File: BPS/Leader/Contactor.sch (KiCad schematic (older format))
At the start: 20 parts, among them J8 ContactorConn, Q1 NTR4003NT1G, Q2 VND5N07-E, U8 SI8261ABC-IS, U9 BAS70-04

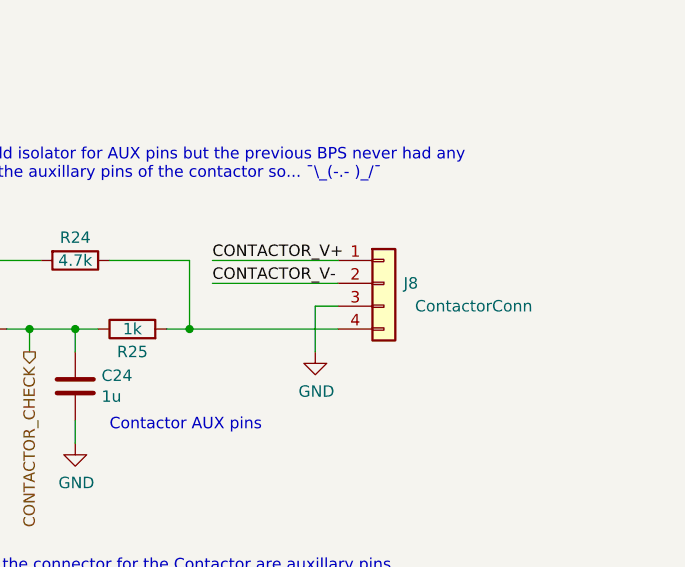
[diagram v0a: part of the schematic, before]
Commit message: Places most components of leader board in their respective locations with nothing traced
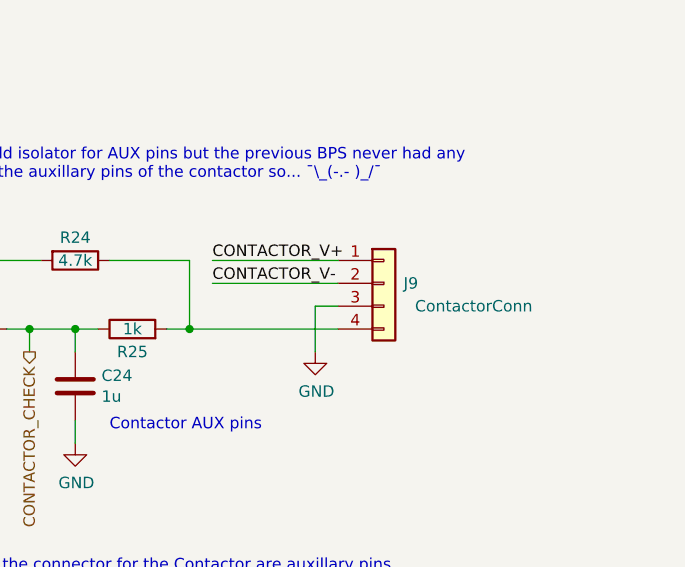
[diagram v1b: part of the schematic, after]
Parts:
- renumbered J8 to J9
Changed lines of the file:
@@
 $EndDescr
 $Comp
-L Connector_Generic:Conn_01x04 J8
+L Connector_Generic:Conn_01x04 J9
 U 1 1 5C2DA595
 P 10050 3500
-F 0 "J8" H 10200 3500 50  0000 R CNN
+F 0 "J9" H 10200 3500 50  0000 R CNN
 F 1 "ContactorConn" H 10700 3400 50  0000 R CNN
 F 2 "UTSVT_Connectors:Molex_MicroFit3.0_1x4xP3.00mm_PolarizingPeg_Vertical" H 10050 3500 50  0001 C CNN

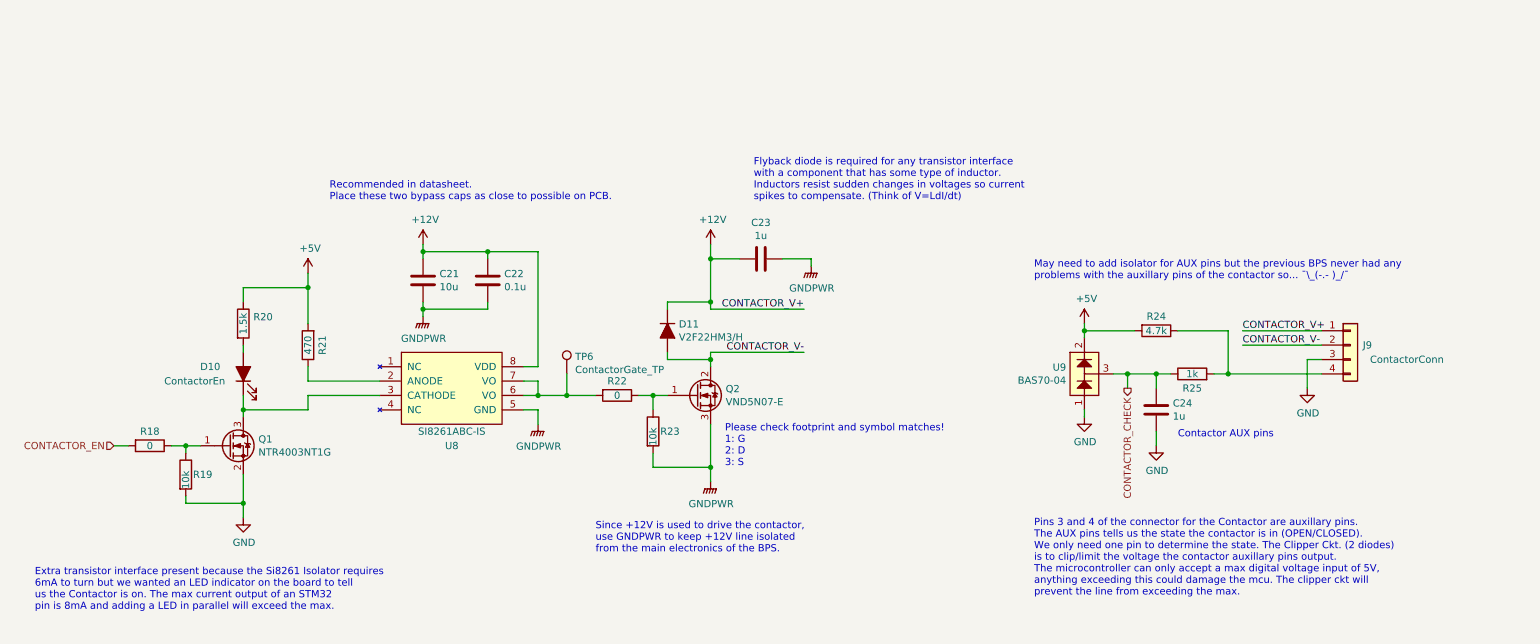
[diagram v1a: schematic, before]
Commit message: Adds power planes
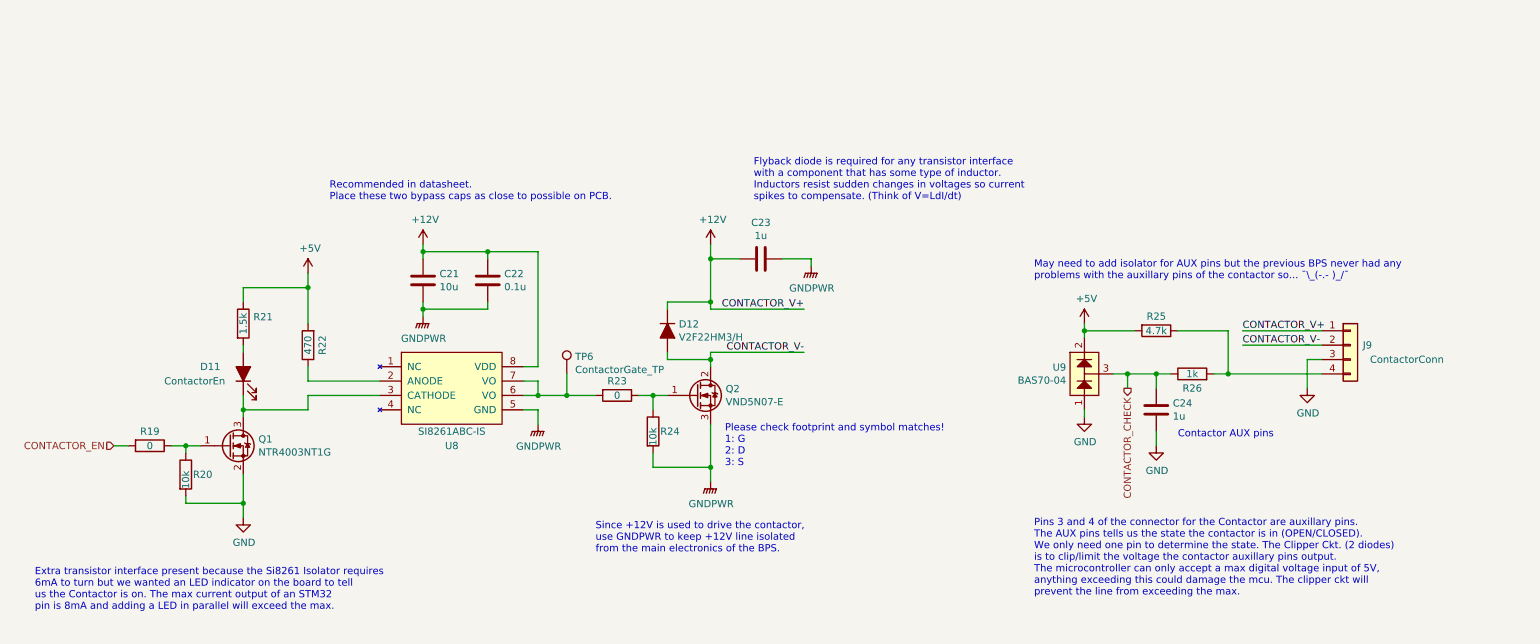
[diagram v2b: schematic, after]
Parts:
- renumbered D10 to D11, D11 to D12, R18 to R19, R19 to R20, R20 to R21, R21 to R22, R22 to R23, R23 to R24, R24 to R25, R25 to R26
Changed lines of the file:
@@
 $EndComp
 $Comp
-L Device:R R25
+L Device:R R26
 U 1 1 5C302C24
 P 8950 3700
-F 0 "R25" V 8850 3700 50  0000 C CNN
+F 0 "R26" V 8850 3700 50  0000 C CNN
 F 1 "1k" V 8950 3700 50  0000 C CNN
 F 2 "Resistor_SMD:R_0805_2012Metric" V 8880 3700 50  0001 C CNN
@@
 CONTACTOR_V-
 $Comp
-L Device:R R23
+L Device:R R24
 U 1 1 5C30E2C4
 P 5200 4100
-F 0 "R23" H 5250 4100 50  0000 L CNN
+F 0 "R24" H 5250 4100 50  0000 L CNN
 F 1 "10k" V 5200 4000 50  0000 L CNN
 F 2 "Resistor_SMD:R_0805_2012Metric" V 5130 4100 50  0001 C CNN
@@
 Connection ~ 5600 4350
 $Comp
-L Device:R R22
+L Device:R R23
 U 1 1 5C30EC57
 P 4950 3850
-F 0 "R22" V 4850 3850 50  0000 C CNN
+F 0 "R23" V 4850 3850 50  0000 C CNN
 F 1 "0" V 4950 3850 50  0000 C CNN
 F 2 "Resistor_SMD:R_0805_2012Metric" V 4880 3850 50  0001 C CNN
@@
 	4400 3950 4300 3950
 $Comp
-L Device:R R21
+L Device:R R22
 U 1 1 5C3152A3
 P 2800 3500
-F 0 "R21" V 2700 3500 50  0000 C CNN
+F 0 "R22" V 2700 3500 50  0000 C CNN
 F 1 "470" V 2800 3500 50  0000 C CNN
 F 2 "Resistor_SMD:R_0805_2012Metric" V 2730 3500 50  0001 C CNN
@@
 Please check footprint and symbol matches!\n1: G\n2: D\n3: S
 $Comp
-L Device:D_ALT D11
+L Device:D_ALT D12
 U 1 1 5C31D45E
 P 5300 3400
-F 0 "D11" V 5254 3479 50  0000 L CNN
+F 0 "D12" V 5254 3479 50  0000 L CNN
 F 1 "V2F22HM3/H" V 5345 3479 50  0000 L CNN
 F 2 "UTSVT_Passive:V2F22HM" H 5300 3400 50  0001 C CNN
@@
 Connection ~ 4600 3850
 $Comp
-L Device:R R20
+L Device:R R21
 U 1 1 5C381FF3
 P 2350 3350
-F 0 "R20" H 2420 3396 50  0000 L CNN
+F 0 "R21" H 2420 3396 50  0000 L CNN
 F 1 "1.5k" V 2350 3350 50  0000 C CNN
 F 2 "Resistor_SMD:R_0805_2012Metric" V 2280 3350 50  0001 C CNN
@@
 	2350 3200 2350 3100
 $Comp
-L Device:LED_ALT D10
+L Device:LED_ALT D11
 U 1 1 5C382DF7
 P 2350 3700
-F 0 "D10" V 2400 4000 50  0000 R CNN
+F 0 "D11" V 2400 4000 50  0000 R CNN
 F 1 "ContactorEn" V 2300 4250 50  0000 R CNN
 F 2 "LED_SMD:LED_0805_2012Metric" H 2350 3700 50  0001 C CNN
@@
 	2350 3550 2350 3500
 $Comp
-L Device:R R24
+L Device:R R25
 U 1 1 5C3945DD
 P 8700 3400
-F 0 "R24" V 8600 3400 50  0000 C CNN
+F 0 "R25" V 8600 3400 50  0000 C CNN
 F 1 "4.7k" V 8700 3400 50  0000 C CNN
 F 2 "Resistor_SMD:R_0805_2012Metric" V 8630 3400 50  0001 C CNN
@@
 Connection ~ 2800 3100
 $Comp
-L Device:R R18
+L Device:R R19
 U 1 1 5C3FA547
 P 1700 4200
-F 0 "R18" V 1600 4200 50  0000 C CNN
+F 0 "R19" V 1600 4200 50  0000 C CNN
 F 1 "0" V 1700 4200 50  0000 C CNN
 F 2 "Resistor_SMD:R_0805_2012Metric" V 1630 4200 50  0001 C CNN
@@
 $EndComp
 $Comp
-L Device:R R19
+L Device:R R20
 U 1 1 5C400FAD
 P 1950 4400
-F 0 "R19" H 2000 4400 50  0000 L CNN
+F 0 "R20" H 2000 4400 50  0000 L CNN
 F 1 "10k" V 1950 4300 50  0000 L CNN
 F 2 "Resistor_SMD:R_0805_2012Metric" V 1880 4400 50  0001 C CNN

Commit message: Finished leader board
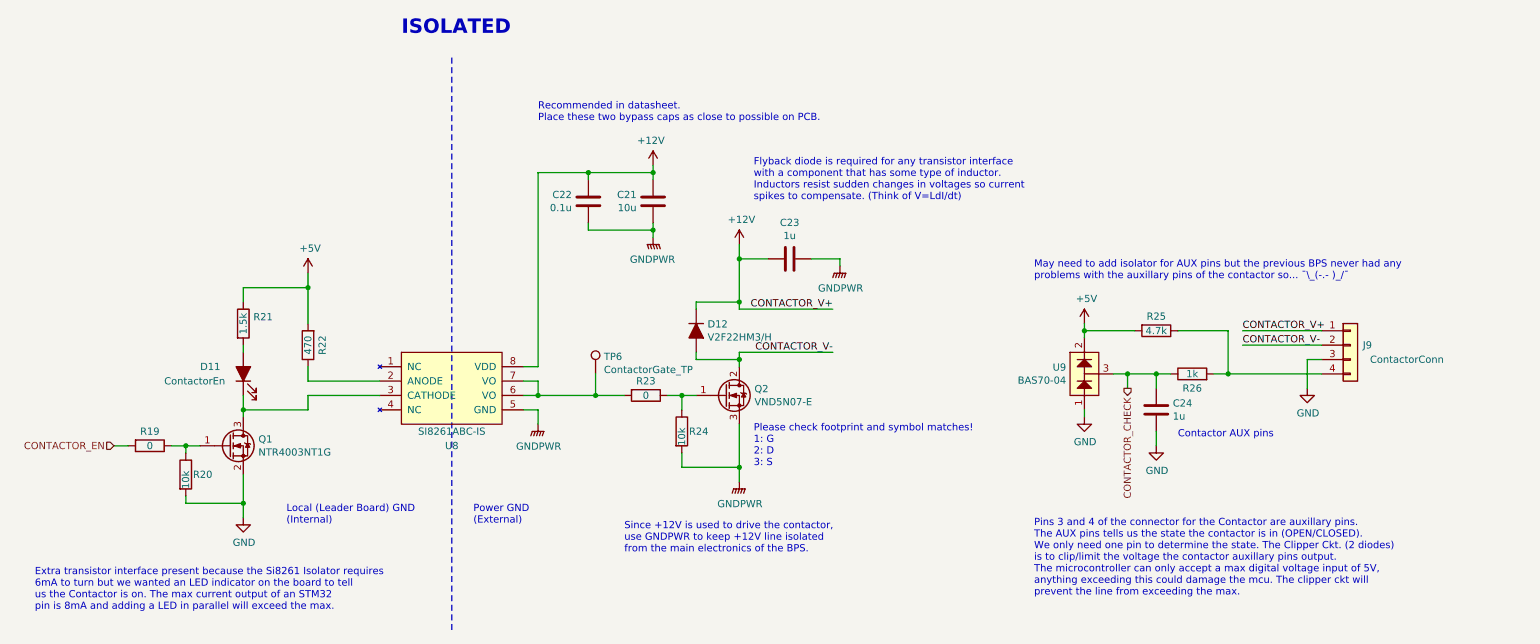
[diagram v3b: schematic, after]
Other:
- note added: "ISOLATED"
- note added: "Local (Leader Board) GND\n(Internal)"
- note added: "Power GND\n(External)"
- moved on the sheet: C21, C22, C23, D12, Q2, R23, R24, TP6

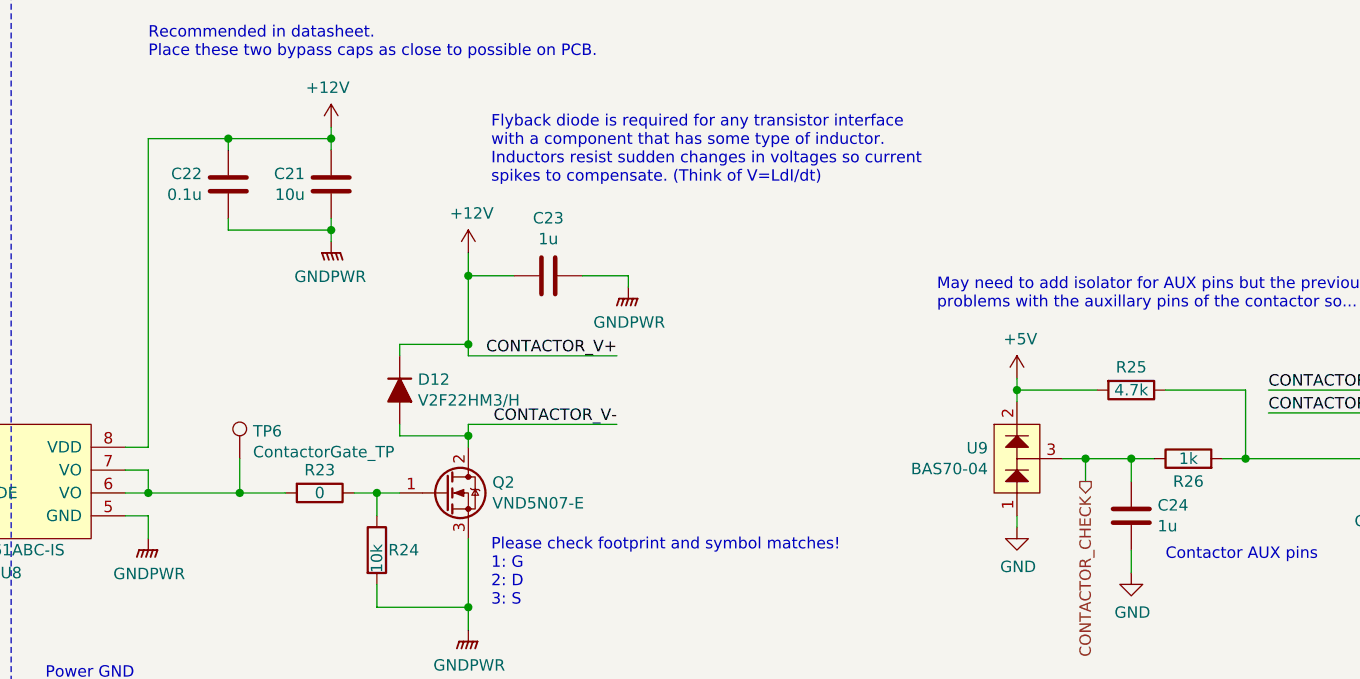
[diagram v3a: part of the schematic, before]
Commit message: Simplifies dc-dc converter schematics
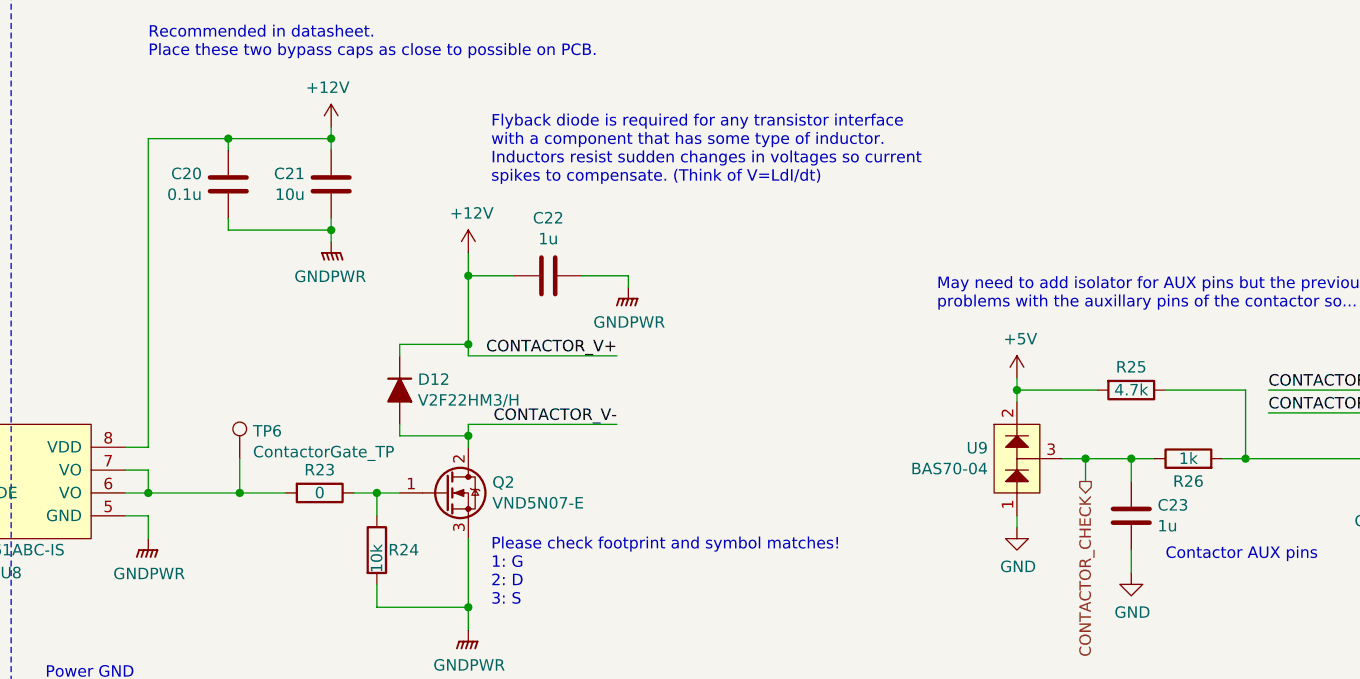
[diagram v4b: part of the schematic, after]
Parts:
- renumbered C22 to C20, C23 to C22, C24 to C23
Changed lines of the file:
@@
 $EndComp
 $Comp
-L power:GND #PWR062
+L power:GND #PWR061
 U 1 1 5C30292A
 P 9750 3800
-F 0 "#PWR062" H 9750 3550 50  0001 C CNN
+F 0 "#PWR061" H 9750 3550 50  0001 C CNN
 F 1 "GND" H 9755 3627 50  0000 C CNN
 F 2 "" H 9750 3800 50  0001 C CNN
@@
 	9850 3700 9200 3700
 $Comp
-L Device:C C24
+L Device:C C23
 U 1 1 5C3030F2
 P 8700 3950
-F 0 "C24" H 8815 3996 50  0000 L CNN
+F 0 "C23" H 8815 3996 50  0000 L CNN
 F 1 "1u" H 8815 3905 50  0000 L CNN
 F 2 "Capacitor_SMD:C_0805_2012Metric" H 8738 3800 50  0001 C CNN
@@
 	8700 4200 8700 4100
 $Comp
-L power:GND #PWR061
+L power:GND #PWR060
 U 1 1 5C304D16
 P 8700 4200
-F 0 "#PWR061" H 8700 3950 50  0001 C CNN
+F 0 "#PWR060" H 8700 3950 50  0001 C CNN
 F 1 "GND" H 8705 4027 50  0000 C CNN
 F 2 "" H 8700 4200 50  0001 C CNN
@@
 Connection ~ 8700 3700
 $Comp
-L power:GND #PWR060
+L power:GND #PWR059
 U 1 1 5C305432
 P 8200 4000
-F 0 "#PWR060" H 8200 3750 50  0001 C CNN
+F 0 "#PWR059" H 8200 3750 50  0001 C CNN
 F 1 "GND" H 8205 3827 50  0000 C CNN
 F 2 "" H 8200 4000 50  0001 C CNN
@@
 	8200 4000 8200 3950
 $Comp
-L power:+5V #PWR059
+L power:+5V #PWR058
 U 1 1 5C305723
 P 8200 3350
-F 0 "#PWR059" H 8200 3200 50  0001 C CNN
+F 0 "#PWR058" H 8200 3200 50  0001 C CNN
 F 1 "+5V" H 8215 3523 50  0000 C CNN
 F 2 "" H 8200 3350 50  0001 C CNN
@@
 	9200 3700 9100 3700
 $Comp
-L power:GNDPWR #PWR057
+L power:GNDPWR #PWR056
 U 1 1 5C3F7F9B
 P 5800 4450
-F 0 "#PWR057" H 5800 4250 50  0001 C CNN
+F 0 "#PWR056" H 5800 4250 50  0001 C CNN
 F 1 "GNDPWR" H 5804 4296 50  0000 C CNN
 F 2 "" H 5800 4400 50  0001 C CNN
@@
 $EndComp
 $Comp
-L power:GNDPWR #PWR055
+L power:GNDPWR #PWR052
 U 1 1 5C3FD54A
 P 4400 4050
-F 0 "#PWR055" H 4400 3850 50  0001 C CNN
+F 0 "#PWR052" H 4400 3850 50  0001 C CNN
 F 1 "GNDPWR" H 4404 3896 50  0000 C CNN
 F 2 "" H 4400 4000 50  0001 C CNN
@@
 P 2350 4700
 AR Path="/5C392C6A/5C9B866F" Ref="#PWR?"  Part="1"
-AR Path="/5C38C674/5C9B866F" Ref="#PWR051"  Part="1"
-F 0 "#PWR051" H 2350 4450 50  0001 C CNN
+AR Path="/5C38C674/5C9B866F" Ref="#PWR050"  Part="1"
+F 0 "#PWR050" H 2350 4450 50  0001 C CNN
 F 1 "GND" H 2355 4527 50  0000 C CNN
 F 2 "" H 2350 4700 50  0001 C CNN
@@
 	2350 3950 2350 4000
 $Comp
-L power:+5V #PWR052
+L power:+5V #PWR051
 U 1 1 5C3C25EA
 P 2800 3000
-F 0 "#PWR052" H 2800 2850 50  0001 C CNN
+F 0 "#PWR051" H 2800 2850 50  0001 C CNN
 F 1 "+5V" H 2815 3173 50  0000 C CNN
 F 2 "" H 2800 3000 50  0001 C CNN
@@
 	4400 3750 4400 3850
 $Comp
-L power:+12V #PWR056
+L power:+12V #PWR055
 U 1 1 5C30CB9C
 P 5800 2800
-F 0 "#PWR056" H 5800 2650 50  0001 C CNN
+F 0 "#PWR055" H 5800 2650 50  0001 C CNN
 F 1 "+12V" H 5815 2973 50  0000 C CNN
 F 2 "" H 5800 2800 50  0001 C CNN
@@
 	6500 2950 6500 2900
 $Comp
-L power:GNDPWR #PWR058
+L power:GNDPWR #PWR057
 U 1 1 5C3F88F8
 P 6500 2950
-F 0 "#PWR058" H 6500 2750 50  0001 C CNN
+F 0 "#PWR057" H 6500 2750 50  0001 C CNN
 F 1 "GNDPWR" H 6504 2796 50  0000 C CNN
 F 2 "" H 6500 2900 50  0001 C CNN
@@
 	6000 2900 5800 2900
 $Comp
-L Device:C C23
+L Device:C C22
 U 1 1 5C3F87F6
 P 6150 2900
-F 0 "C23" V 5898 2900 50  0000 C CNN
+F 0 "C22" V 5898 2900 50  0000 C CNN
 F 1 "1u" V 5989 2900 50  0000 C CNN
 F 2 "Capacitor_SMD:C_0805_2012Metric" H 6188 2750 50  0001 C CNN
@@
 	5200 2750 5200 2700
 $Comp
-L Device:C C22
+L Device:C C20
 U 1 1 5C310937
 P 4750 2500
-F 0 "C22" H 4865 2546 50  0000 L CNN
+F 0 "C20" H 4865 2546 50  0000 L CNN
 F 1 "0.1u" H 4865 2455 50  0000 L CNN
 F 2 "Capacitor_SMD:C_0805_2012Metric" H 4788 2350 50  0001 C CNN
